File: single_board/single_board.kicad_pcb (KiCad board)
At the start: 4 copper layers, 118.6 x 108.9 mm, 120 parts, among them J1 SWD, J11 SPI Debug, J17 BOOTSEL, J2 USB_C_Receptacle_USB2.0_16P, J3 RST, J30 JST_GH_H, J31 JST_GH_H, J32 PB_Vertical, J33 JST_GH_H, J34 PB_Vertical, J35 JST_GH_H, J36 JST_GH_H, J37 JST_GH_H, J38 PB_Vertical, J39 PB_Vertical, J4 Conn_01x02, J40 PB_Vertical, J41 PB_Vertical, J42 PB_Vertical, J43 PB_Vertical, J44 PB_Vertical, J45 PB_Vertical, J46 PB_Vertical, J47 PB_Vertical, J48 PB_Vertical, J49 PB_Vertical, J5 Conn_01x02, J51 JST_GH_H, J6 Conn_01x02, Q1 AO3401A, Q2 AO3401A, Q3 AO3401A, Q4 AO3401A, Q5 2N7002, SW1 Button, U1 AP2112K-3.3, U3 USBLC6-2SC6, U4 LSM6DSV, U5 STM32G474VBTx, Y1 FC-135

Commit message: Setup
Minor adjustments before handoff
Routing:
- net /UART5_RX: track 0.00 -> 4.76 mm
- net /UART5_TX: track 0.00 -> 4.22 mm
- net /IMU_MISO: track 0.00 -> 4.21 mm
- net /IMU_SCK: track 0.00 -> 4.09 mm
- net /UART4_RX: track 0.00 -> 4.04 mm
- net /IMU_MOSI: track 0.00 -> 4.00 mm
- net /IMU_NSS: track 0.00 -> 3.99 mm
- net /UART4_TX: track 0.00 -> 3.63 mm
- net /SWCLK: track 0.00 -> 3.33 mm
- net /TRI_LED_R: track 0.00 -> 3.23 mm
- net /TRI_LED_G: track 0.00 -> 3.23 mm
- net /TRI_LED_B: track 0.00 -> 3.13 mm
- net /INT1: track 0.00 -> 3.08 mm
- net /SWDIO: track 0.00 -> 2.99 mm
- net /INT2: track 0.00 -> 2.59 mm
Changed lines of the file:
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@@
+	)
+	(segment
+		(start 151.025 103.175)
+		(end 151.05 103.15)
+		(width 0.15)
+		(layer "F.Cu")
+		(net "/TRI_LED_R")
+	)
+	(segment
+		(start 151.025 106.365)
+		(end 151.025 103.175)
+		(width 0.15)
+		(layer "F.Cu")
+		(net "/TRI_LED_R")
 	)
 	(segment
@@
 	)
 	(segment
+		(start 149.525 106.365)
+		(end 149.525 102.375)
+		(width 0.15)
+		(layer "F.Cu")
+		(net "/IMU_NSS")
+	)
+	(segment
+		(start 149.025 106.365)
+		(end 149.025 102.275)
+		(width 0.15)
+		(layer "F.Cu")
+		(net "/IMU_SCK")
+	)
+	(segment
+		(start 148.025 106.365)
+		(end 148.025 102.825)
+		(width 0.15)
+		(layer "F.Cu")
+		(net "/IMU_MOSI")
+	)
+	(segment
+		(start 148.025 102.825)
+		(end 147.7 102.5)
+		(width 0.15)
+		(layer "F.Cu")
+		(net "/IMU_MOSI")
+	)
+	(segment
+		(start 148.525 106.365)
+		(end 148.525 102.475)
+		(width 0.15)
+		(layer "F.Cu")
+		(net "/IMU_MISO")
+	)
+	(segment
+		(start 148.525 102.475)
+		(end 148.3 102.25)
+		(width 0.15)
+		(layer "F.Cu")
+		(net "/IMU_MISO")
+	)
+	(segment
 		(start 160.34 119.04)
 		(end 165.75 124.45)
@@
 		(layer "F.Cu")
 		(net "/PWM2")
+	)
+	(segment
+		(start 152.025 106.365)
+		(end 152.025 104.325)
+		(width 0.15)
+		(layer "F.Cu")
+		(net "/UART5_RX")
+	)
+	(segment
+		(start 152.025 104.325)
+		(end 153.95 102.4)
+		(width 0.15)
+		(layer "F.Cu")
+		(net "/UART5_RX")
+	)
+	(segment
+		(start 153.525 103.525)
+		(end 154.5 102.55)
+		(width 0.15)
+		(layer "F.Cu")
+		(net "/UART5_TX")
+	)
+	(segment
+		(start 153.525 106.365)
+		(end 153.525 103.525)
+		(width 0.15)
+		(layer "F.Cu")
+		(net "/UART5_TX")
 	)
 	(segment
@@
 	)
 	(segment
+		(start 147.525 106.365)
+		(end 147.525 103.675)
+		(width 0.15)
+		(layer "F.Cu")
+		(net "/INT1")
+	)
+	(segment
+		(start 147.525 103.675)
+		(end 147.25 103.4)
+		(width 0.15)
+		(layer "F.Cu")
+		(net "/INT1")
+	)
+	(segment
+		(start 150.025 106.365)
+		(end 150.025 103.775)
+		(width 0.15)
+		(layer "F.Cu")
+		(net "/INT2")
+	)
+	(segment
+		(start 154.025 106.365)
+		(end 154.025 103.775)
+		(width 0.15)
+		(layer "F.Cu")
+		(net "/UART4_RX")
+	)
+	(segment
+		(start 154.025 103.775)
+		(end 155.05 102.75)
+		(width 0.15)
+		(layer "F.Cu")
+		(net "/UART4_RX")
+	)
+	(segment
+		(start 154.525 106.365)
+		(end 154.525 103.975)
+		(width 0.15)
+		(layer "F.Cu")
+		(net "/UART4_TX")
+	)
+	(segment
+		(start 154.525 103.975)
+		(end 155.4 103.1)
+		(width 0.15)
+		(layer "F.Cu")
+		(net "/UART4_TX")
+	)
+	(segment
 		(start 152.525 126.825)
 		(end 152.6 126.9)
@@
 	)
 	(segment
+		(start 150.525 103.275)
+		(end 150.55 103.25)
+		(width 0.15)
+		(layer "F.Cu")
+		(net "/TRI_LED_B")
+	)
+	(segment
+		(start 150.525 106.365)
+		(end 150.525 103.275)
+		(width 0.15)
+		(layer "F.Cu")
+		(net "/TRI_LED_B")
+	)
+	(segment
 		(start 142.35 117.54)
 		(end 135.46 117.54)
@@
 		(net "/CAN_TX")
 	)
+	(segment
+		(start 156.025 105.175)
+		(end 157.3 103.9)
+		(width 0.15)
+		(layer "F.Cu")
+		(net "/SWDIO")
+	)
+	(segment
+		(start 156.025 106.365)
+		(end 156.025 105.175)
+		(width 0.15)
+		(layer "F.Cu")
+		(net "/SWDIO")
+	)
+	(segment
+		(start 155.525 104.975)
+		(end 156.9 103.6)
+		(width 0.15)
+		(layer "F.Cu")
+		(net "/SWCLK")
+	)
+	(segment
+		(start 155.525 106.365)
+		(end 155.525 104.975)
+		(width 0.15)
+		(layer "F.Cu")
+		(net "/SWCLK")
+	)
+	(segment
+		(start 151.525 103.175)
+		(end 151.55 103.15)
+		(width 0.15)
+		(layer "F.Cu")
+		(net "/TRI_LED_G")
+	)
+	(segment
+		(start 151.525 106.365)
+		(end 151.525 103.175)
+		(width 0.15)
+		(layer "F.Cu")
+		(net "/TRI_LED_G")
+	)
 	(zone

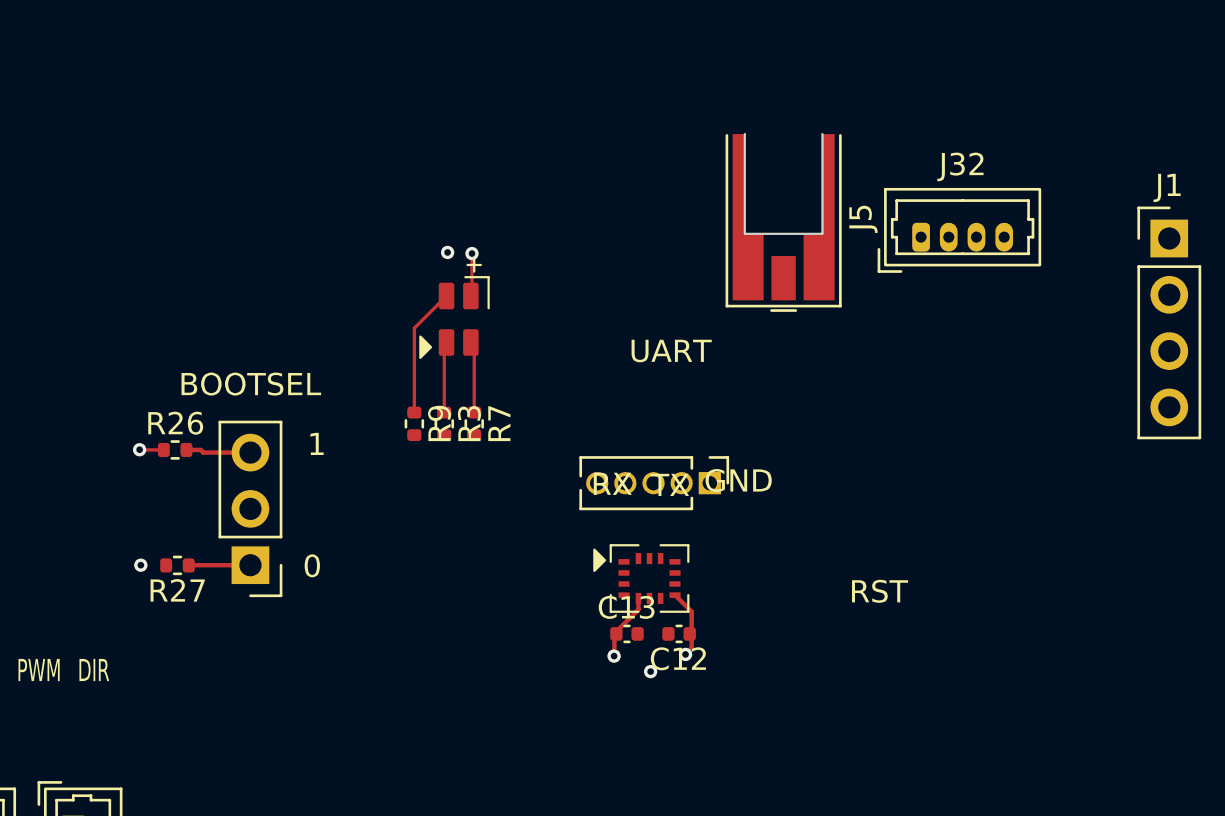
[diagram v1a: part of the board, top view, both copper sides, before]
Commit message: Updated connectors
2MMCX for comms uart, picoblade for i2c
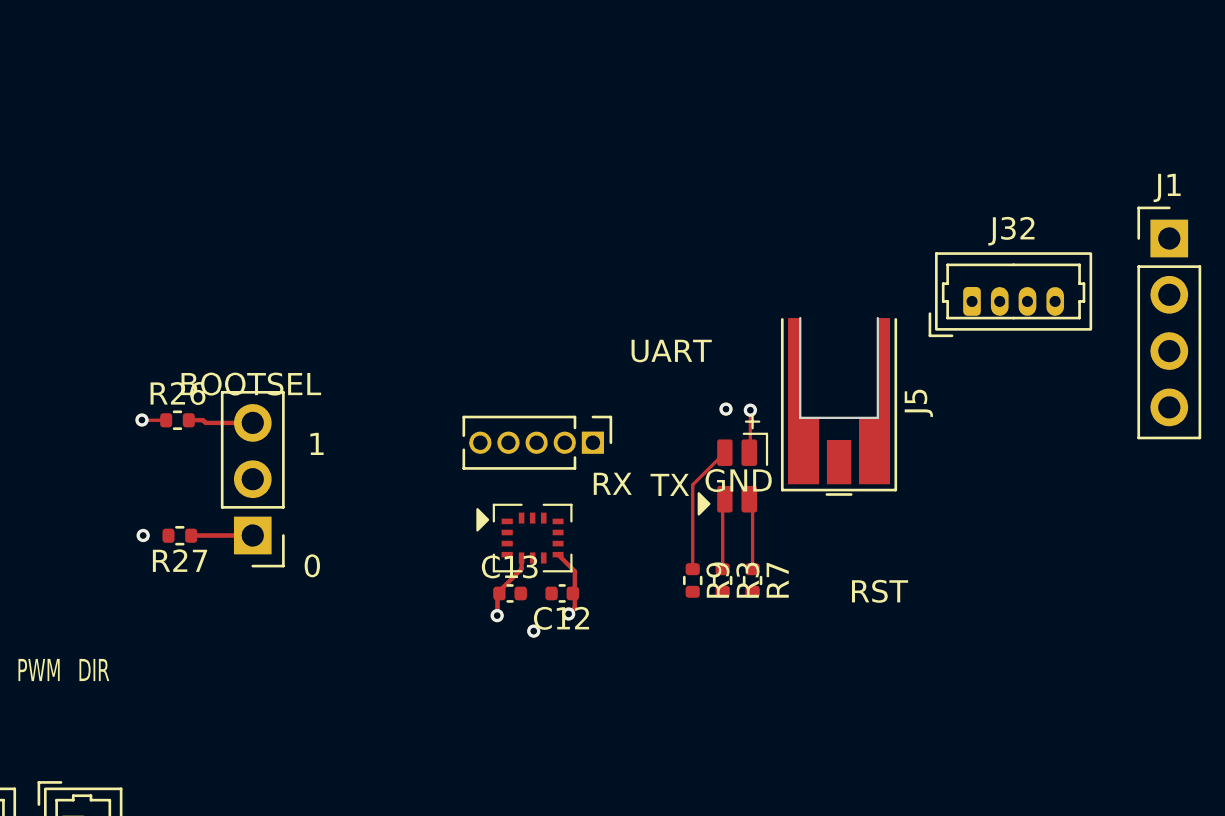
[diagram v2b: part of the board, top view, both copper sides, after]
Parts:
- moved D3 14.4 mm to (153.4, 85.2)
- moved R3 14.4 mm to (152.8, 89.9)
- moved R7 14.4 mm to (154.1, 89.9)
- moved R9 14.4 mm to (151.4, 89.9)
- moved J5 8.67 mm to (158.0, 81.8)
- moved C13 5.58 mm to (143.2, 90.5)
- moved C12 5.58 mm to (145.5, 90.5)
- moved J11 5.58 mm to (146.9, 83.7)
- moved U4 5.58 mm to (144.2, 88.0)
- moved J32 3.70 mm to (164.0, 77.3)
- moved J17 1.34 mm to (131.6, 87.9)
- moved R26 1.34 mm to (128.2, 82.7)
- moved R27 1.34 mm to (128.3, 87.9)
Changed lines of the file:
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@@
 	(footprint "Rover:FM-B2020RGBA-HG Hand Solder"
 		(layer "F.Cu")
-		(at 140.84 78.105 -90)
+		(at 153.4 85.1725 -90)
 		(property "Reference" "D3"
 			(at 0 -2.6 270)
@@
 	(footprint "Connector_PinHeader_2.54mm:PinHeader_1x03_P2.54mm_Vertical"
 		(layer "F.Cu")
-		(at 131.445 89.2 180)
+		(at 131.55 87.86 180)
 		(descr "Through hole straight pin header, 1x03, 2.54mm pitch, single row")
 		(tags "Through hole pin header THT 1x03 2.54mm single row")
@@
 	(footprint "Capacitor_SMD:C_0402_1005Metric"
 		(layer "F.Cu")
-		(at 148.4325 92.3)
+		(at 143.158235 90.474265)
 		(descr "Capacitor SMD 0402 (1005 Metric), square (rectangular) end terminal, IPC-7351 nominal, (Body size source: IPC-SM-782 page 76, https://www.pcb-3d.com/wordpress/wp-content/uploads/ipc-sm-782a_amendment_1_and_2.pdf)")
 		(tags "capacitor")
@@
 	(footprint "Resistor_SMD:R_0402_1005Metric"
 		(layer "F.Cu")
-		(at 128.0475 84)
+		(at 128.1525 82.66)
 		(descr "Resistor SMD 0402 (1005 Metric), square (rectangular) end terminal, IPC-7351 nominal, (Body size source: IPC-SM-782 page 72, https://www.pcb-3d.com/wordpress/wp-content/uploads/ipc-sm-782a_amendment_1_and_2.pdf)")
 		(tags "resistor")
@@
 	(footprint "Resistor_SMD:R_0402_1005Metric"
 		(layer "F.Cu")
-		(at 140.19 82.8225 -90)
+		(at 152.75 89.89 -90)
 		(descr "Resistor SMD 0402 (1005 Metric), square (rectangular) end terminal, IPC-7351 nominal, (Body size source: IPC-SM-782 page 72, https://www.pcb-3d.com/wordpress/wp-content/uploads/ipc-sm-782a_amendment_1_and_2.pdf)")
 		(tags "resistor")
@@
 	(footprint "Capacitor_SMD:C_0402_1005Metric"
 		(layer "F.Cu")
-		(at 150.7825 92.3 180)
+		(at 145.508235 90.474265 180)
 		(descr "Capacitor SMD 0402 (1005 Metric), square (rectangular) end terminal, IPC-7351 nominal, (Body size source: IPC-SM-782 page 76, https://www.pcb-3d.com/wordpress/wp-content/uploads/ipc-sm-782a_amendment_1_and_2.pdf)")
 		(tags "capacitor")
@@
 	(footprint "Connector_PinHeader_1.27mm:PinHeader_1x05_P1.27mm_Vertical"
 		(layer "F.Cu")
-		(at 152.17 85.5 -90)
+		(at 146.895735 83.674265 -90)
 		(descr "Through hole straight pin header, 1x05, 1.27mm pitch, single row")
 		(tags "Through hole pin header THT 1x05 1.27mm single row")
@@
 	(footprint "Connector_Coaxial:MMCX_Molex_73415-0961_Horizontal_0.8mm-PCB"
 		(layer "F.Cu")
-		(at 155.5 73.5 -90)
+		(at 158 81.8 -90)
 		(descr "Molex MMCX Horizontal Coaxial https://www.molex.com/pdm_docs/sd/734150961_sd.pdf")
 		(tags "Molex MMCX Horizontal Coaxial")
@@
 	(footprint "Rover:LSM6DSV"
 		(layer "F.Cu")
-		(at 149.45 89.8)
+		(at 144.175735 87.974265)
 		(property "Reference" "U4"
 			(at 0 -3.2 0)
@@
 	(footprint "Connector_Molex:Molex_PicoBlade_53047-0410_1x04_P1.25mm_Vertical"
 		(layer "F.Cu")
-		(at 161.7 74.4)
+		(at 164 77.3)
 		(descr "Molex PicoBlade Connector System, 53047-0410, 4 Pins per row (http://www.molex.com/pdm_docs/sd/530470610_sd.pdf)")
 		(tags "connector Molex PicoBlade vertical")
@@
 	(footprint "Resistor_SMD:R_0402_1005Metric"
 		(layer "F.Cu")
-		(at 138.84 82.8225 -90)
+		(at 151.4 89.89 -90)
 		(descr "Resistor SMD 0402 (1005 Metric), square (rectangular) end terminal, IPC-7351 nominal, (Body size source: IPC-SM-782 page 72, https://www.pcb-3d.com/wordpress/wp-content/uploads/ipc-sm-782a_amendment_1_and_2.pdf)")
 		(tags "resistor")
@@
 	(footprint "Resistor_SMD:R_0402_1005Metric"
 		(layer "F.Cu")
-		(at 128.1525 89.21 180)
+		(at 128.2575 87.87 180)
 		(descr "Resistor SMD 0402 (1005 Metric), square (rectangular) end terminal, IPC-7351 nominal, (Body size source: IPC-SM-782 page 72, https://www.pcb-3d.com/wordpress/wp-content/uploads/ipc-sm-782a_amendment_1_and_2.pdf)")
 		(tags "resistor")
@@
 	(footprint "Resistor_SMD:R_0402_1005Metric"
 		(layer "F.Cu")
-		(at 141.54 82.8225 -90)
+		(at 154.1 89.89 -90)
 		(descr "Resistor SMD 0402 (1005 Metric), square (rectangular) end terminal, IPC-7351 nominal, (Body size source: IPC-SM-782 page 72, https://www.pcb-3d.com/wordpress/wp-content/uploads/ipc-sm-782a_amendment_1_and_2.pdf)")
 		(tags "resistor")
@@
 	)
 	(via
-		(at 149.5 94)
+		(at 144.225735 92.174265)
 		(size 0.6)
 		(drill 0.3)
@@
 	)
 	(via
-		(at 126.5 89.2)
+		(at 126.605 87.86)
 		(size 0.6)
 		(drill 0.3)
@@
 	)
 	(via
-		(at 140.34 75.09)
+		(at 152.9 82.1575)
 		(size 0.6)
 		(drill 0.3)
@@
 	)
 	(segment
-		(start 141.44 77.005)
-		(end 141.39 77.055)
+		(start 154 84.0725)
+		(end 153.95 84.1225)
 		(width 0.15)
 		(layer "F.Cu")
@@
 	)
 	(segment
-		(start 151.35 92.95)
-		(end 151.074265 93.225735)
+		(start 146.075735 91.124265)
+		(end 145.8 91.4)
 		(width 0.2)
 		(layer "F.Cu")
@@
 	)
 	(segment
-		(start 147.865 92.3)
-		(end 147.865 93.285)
+		(start 142.590735 90.474265)
+		(end 142.590735 91.459265)
 		(width 0.2)
 		(layer "F.Cu")
@@
 	)
 	(segment
-		(start 151.35 91.3)
-		(end 150.6 90.55)
+		(start 146.075735 89.474265)
+		(end 145.325735 88.724265)
 		(width 0.2)
 		(layer "F.Cu")
@@
 	)
 	(segment
-		(start 151.35 92.3)
-		(end 151.35 92.95)
+		(start 146.075735 90.474265)
+		(end 146.075735 91.124265)
 		(width 0.2)
 		(layer "F.Cu")
@@
 	)
 	(segment
-		(start 126.455 84)
-		(end 126.445 83.99)
+		(start 126.56 82.66)
+		(end 126.55 82.65)
 		(width 0.15)
 		(layer "F.Cu")
@@
 	)
 	(segment
-		(start 148.95 91.2)
-		(end 148.95 90.7)
+		(start 143.675735 89.374265)
+		(end 143.675735 88.874265)
 		(width 0.2)
 		(layer "F.Cu")
@@
 	)
 	(segment
-		(start 151.35 92.3)
-		(end 151.35 91.3)
+		(start 146.075735 90.474265)
+		(end 146.075735 89.474265)
 		(width 0.2)
 		(layer "F.Cu")
@@
 	)
 	(segment
-		(start 147.865 92.3)
-		(end 147.865 92.285)
+		(start 142.590735 90.474265)
+		(end 142.590735 90.459265)
 		(width 0.2)
 		(layer "F.Cu")
@@
 	)
 	(segment
-		(start 141.44 75.14)
-		(end 141.44 77.005)
+		(start 154 82.2075)
+		(end 154 84.0725)
 		(width 0.15)
 		(layer "F.Cu")
@@
 	)
 	(segment
-		(start 147.865 92.285)
-		(end 148.95 91.2)
+		(start 142.590735 90.459265)
+		(end 143.675735 89.374265)
 		(width 0.2)
 		(layer "F.Cu")
@@
 	)
 	(segment
-		(start 127.45 84)
-		(end 126.455 84)
+		(start 127.555 82.66)
+		(end 126.56 82.66)
 		(width 0.15)
 		(layer "F.Cu")
@@
 	)
 	(segment
-		(start 147.865 93.285)
-		(end 147.85 93.3)
+		(start 142.590735 91.459265)
+		(end 142.575735 91.474265)
 		(width 0.2)
 		(layer "F.Cu")
@@
 	)
 	(via
-		(at 147.85 93.3)
+		(at 142.575735 91.474265)
 		(size 0.6)
 		(drill 0.3)
@@
 	)
 	(via
-		(at 151.074265 93.225735)
+		(at 145.8 91.4)
 		(size 0.6)
 		(drill 0.3)
@@
 	)
 	(via
-		(at 141.44 75.14)
+		(at 154 82.2075)
 		(size 0.6)
 		(drill 0.3)
@@
 	)
 	(via
-		(at 126.445 83.99)
+		(at 126.55 82.65)
 		(size 0.6)
 		(drill 0.3)
@@
 	)
 	(segment
-		(start 140.19 79.255)
-		(end 140.29 79.155)
+		(start 152.75 86.3225)
+		(end 152.85 86.2225)
 		(width 0.15)
 		(layer "F.Cu")
@@
 	)
 	(segment
-		(start 140.19 82.255)
-		(end 140.19 79.255)
+		(start 152.75 89.3225)
+		(end 152.75 86.3225)
 		(width 0.15)
 		(layer "F.Cu")
@@
 	)
 	(segment
-		(start 138.84 78.505)
-		(end 140.29 77.055)
+		(start 151.4 85.5725)
+		(end 152.85 84.1225)
 		(width 0.15)
 		(layer "F.Cu")
@@
 	)
 	(segment
-		(start 138.84 82.255)
-		(end 138.84 78.505)
+		(start 151.4 89.3225)
+		(end 151.4 85.5725)
 		(width 0.15)
 		(layer "F.Cu")
@@
 	)
 	(segment
-		(start 141.54 79.305)
-		(end 141.39 79.155)
+		(start 154.1 86.3725)
+		(end 153.95 86.2225)
 		(width 0.15)
 		(layer "F.Cu")
@@
 	)
 	(segment
-		(start 141.54 82.255)
-		(end 141.54 79.305)
+		(start 154.1 89.3225)
+		(end 154.1 86.3725)
 		(width 0.15)
 		(layer "F.Cu")
@@
 	)
 	(segment
-		(start 131.445 89.2)
-		(end 128.76 89.2)
+		(start 131.55 87.86)
+		(end 128.865 87.86)
 		(width 0.2)
 		(layer "F.Cu")
@@
 	)
 	(segment
-		(start 128.76 89.2)
-		(end 128.75 89.21)
+		(start 128.865 87.86)
+		(end 128.855 87.87)
 		(width 0.2)
 		(layer "F.Cu")
@@
 	)
 	(segment
-		(start 128.665 83.98)
-		(end 128.645 84)
+		(start 128.77 82.64)
+		(end 128.75 82.66)
 		(width 0.2)
 		(layer "F.Cu")
@@
 	)
 	(segment
-		(start 129.2 84)
-		(end 129.32 84.12)
+		(start 129.305 82.66)
+		(end 129.425 82.78)
 		(width 0.2)
 		(layer "F.Cu")
@@
 	)
 	(segment
-		(start 129.32 84.12)
-		(end 131.445 84.12)
+		(start 129.425 82.78)
+		(end 131.55 82.78)
 		(width 0.2)
 		(layer "F.Cu")
@@
 	)
 	(segment
-		(start 128.705 84.06)
-		(end 128.645 84)
+		(start 128.81 82.72)
+		(end 128.75 82.66)
 		(width 0.15)
 		(layer "F.Cu")
@@
 	)
 	(segment
-		(start 128.645 84)
-		(end 129.2 84)
+		(start 128.75 82.66)
+		(end 129.305 82.66)
 		(width 0.2)
 		(layer "F.Cu")

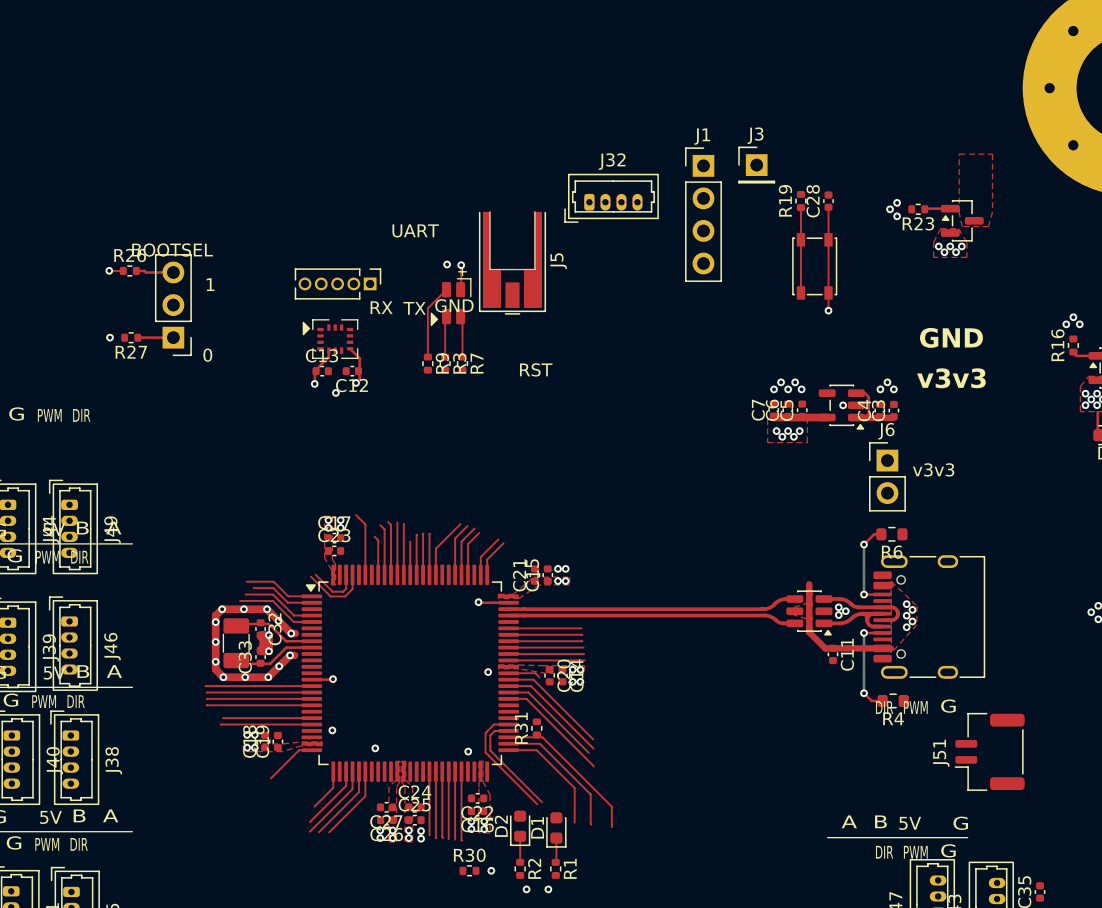
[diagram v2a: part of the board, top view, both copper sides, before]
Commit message: Adjust connector pinouts
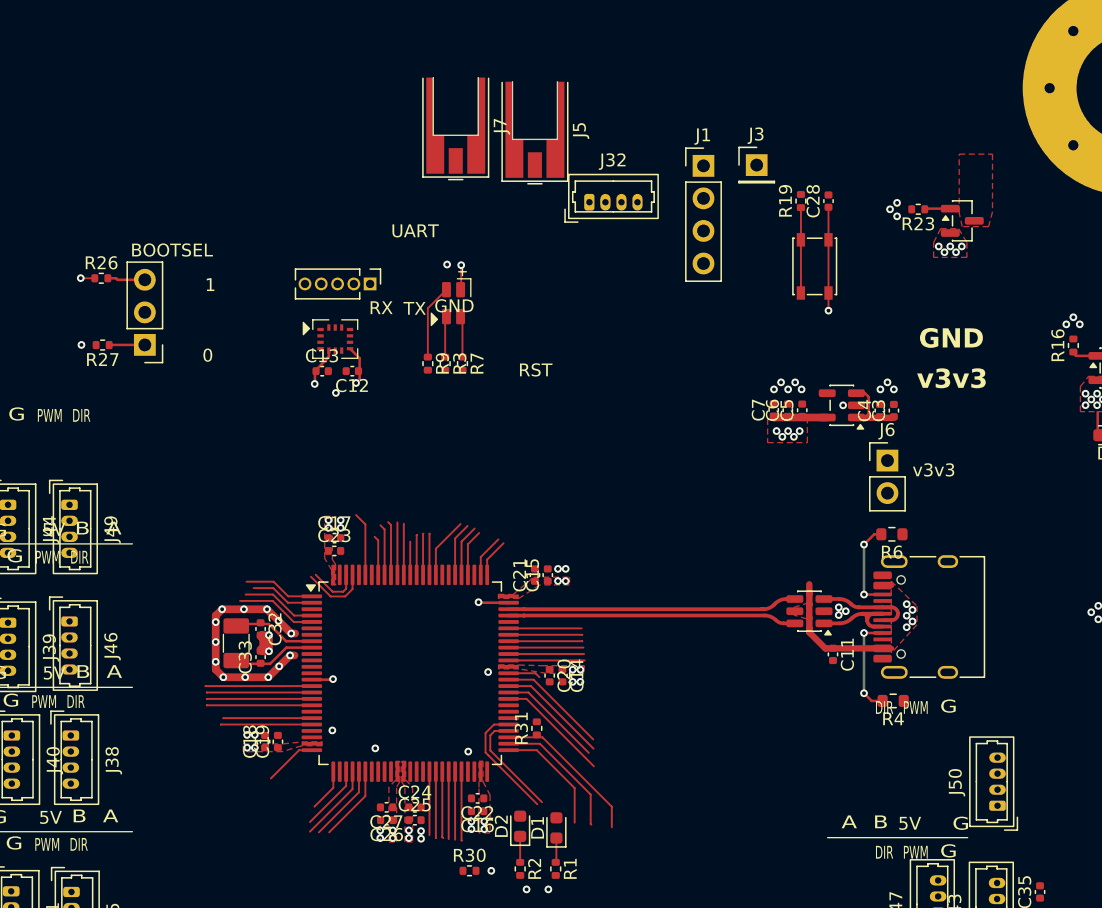
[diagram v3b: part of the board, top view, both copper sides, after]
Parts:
- removed J51: JST_GH_H, Connector_JST:JST_GH_SM02B-GHS-TB_1x02-1MP_P1.25mm_Horizontal
- added J50: PB_Vertical, Connector_Molex:Molex_PicoBlade_53047-0410_1x04_P1.25mm_Vertical, F.Cu at (195.8, 124.4)
- added J7: Conn_01x02, Connector_Coaxial:MMCX_Molex_73415-0961_Horizontal_0.8mm-PCB, F.Cu at (153.6, 71.3)
- moved J5 10.3 mm to (159.8, 71.7)
- moved J17 2.30 mm to (129.3, 88.4)
- moved R26 2.30 mm to (125.9, 83.2)
- moved R27 2.30 mm to (126.0, 88.4)
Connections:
- J32 pad 1: /UART4_RX -> v3v3
- J32 pad 2: /UART4_TX -> /UART4_RX
- J32 pad 3: GND -> /UART4_TX
- J32 pad 4: unconnected-(J32-Pin_4-Pad4) -> GND
- J5 pad 2: /UART5_TX -> GND
